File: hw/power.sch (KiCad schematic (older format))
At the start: 10 parts, among them U10 MCP1826S, U11 MCP1826S

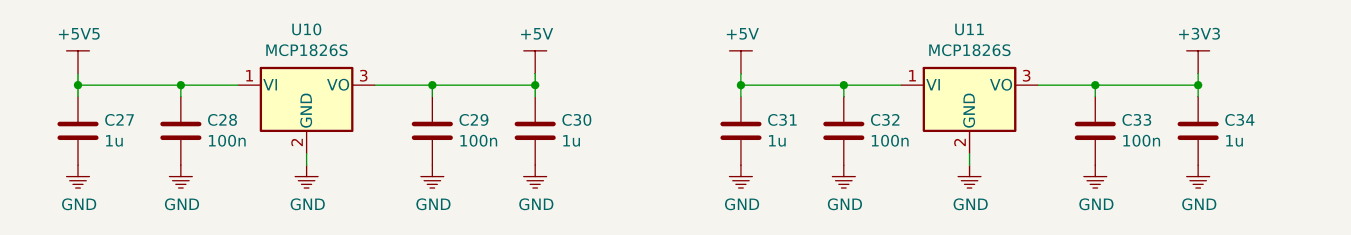
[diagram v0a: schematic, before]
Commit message: updated schematic added footptints
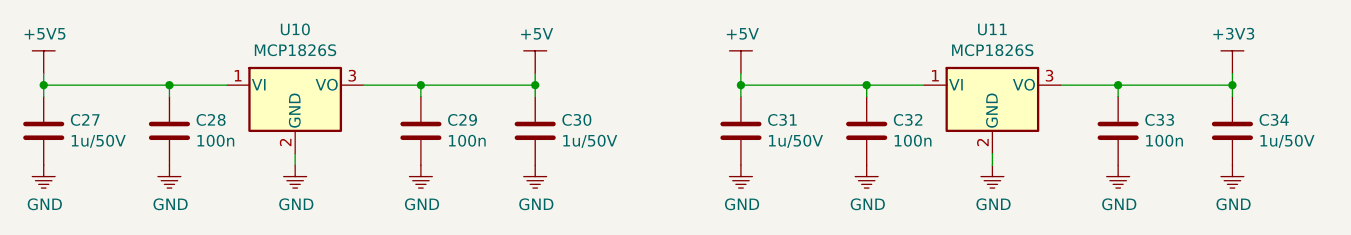
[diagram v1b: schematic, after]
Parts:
- C27, C30, C31, C34: value 1u -> 1u/50V; footprint (none) -> Capacitor_SMD:C_0805_2012Metric
- C28, C29, C32, C33: footprint (none) -> Capacitor_SMD:C_0805_2012Metric
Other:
- moved on the sheet: C27, C28, C29, C32, C33, C34, U10, U11

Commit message: updated schematic
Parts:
- renumbered U11 to U10, U10 to U9
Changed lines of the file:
@@
 $EndDescr
 $Comp
-L Regulator_Linear:MCP1826S U10
+L Regulator_Linear:MCP1826S U9
 U 1 1 5ACF90C5
 P 2650 2300
-F 0 "U10" H 2650 2542 50  0000 C CNN
+F 0 "U9" H 2650 2542 50  0000 C CNN
 F 1 "MCP1826S" H 2650 2451 50  0000 C CNN
 F 2 "Package_TO_SOT_SMD:SOT-223-3_TabPin2" H 2550 2450 50  0001 C CNN
@@
 $EndComp
 $Comp
-L KLIB_Power:GND #PWR068
+L KLIB_Power:GND #PWR067
 U 1 1 5ACF90E8
 P 1550 2650
-F 0 "#PWR068" H 1550 2450 50  0001 C CNN
+F 0 "#PWR067" H 1550 2450 50  0001 C CNN
 F 1 "GND" H 1555 2477 50  0000 C CNN
 F 2 "" H 1550 2650 50  0001 C CNN
@@
 $EndComp
 $Comp
-L KLIB_Power:GND #PWR069
+L KLIB_Power:GND #PWR068
 U 1 1 5ACF90EE
 P 2100 2650
-F 0 "#PWR069" H 2100 2450 50  0001 C CNN
+F 0 "#PWR068" H 2100 2450 50  0001 C CNN
 F 1 "GND" H 2105 2477 50  0000 C CNN
 F 2 "" H 2100 2650 50  0001 C CNN
@@
 $EndComp
 $Comp
-L KLIB_Power:GND #PWR070
+L KLIB_Power:GND #PWR069
 U 1 1 5ACF90F4
 P 2650 2650
-F 0 "#PWR070" H 2650 2450 50  0001 C CNN
+F 0 "#PWR069" H 2650 2450 50  0001 C CNN
 F 1 "GND" H 2655 2477 50  0000 C CNN
 F 2 "" H 2650 2650 50  0001 C CNN
@@
 $EndComp
 $Comp
-L KLIB_Power:GND #PWR071
+L KLIB_Power:GND #PWR070
 U 1 1 5ACF90FA
 P 3200 2650
-F 0 "#PWR071" H 3200 2450 50  0001 C CNN
+F 0 "#PWR070" H 3200 2450 50  0001 C CNN
 F 1 "GND" H 3205 2477 50  0000 C CNN
 F 2 "" H 3200 2650 50  0001 C CNN
@@
 $EndComp
 $Comp
-L KLIB_Power:GND #PWR073
+L KLIB_Power:GND #PWR072
 U 1 1 5ACF9100
 P 3700 2650
-F 0 "#PWR073" H 3700 2450 50  0001 C CNN
+F 0 "#PWR072" H 3700 2450 50  0001 C CNN
 F 1 "GND" H 3705 2477 50  0000 C CNN
 F 2 "" H 3700 2650 50  0001 C CNN
@@
 Connection ~ 3700 2300
 $Comp
-L KLIB_Power:+5V #PWR072
+L KLIB_Power:+5V #PWR071
 U 1 1 5ACF9115
 P 3700 2250
-F 0 "#PWR072" H 3700 1950 50  0001 C CNN
+F 0 "#PWR071" H 3700 1950 50  0001 C CNN
 F 1 "+5V" H 3705 2423 50  0000 C CNN
 F 2 "" H 3700 2250 50  0001 C CNN
@@
 $EndComp
 $Comp
-L KLIB_Power:+5V5 #PWR067
+L KLIB_Power:+5V5 #PWR066
 U 1 1 5ACF911B
 P 1550 2250
-F 0 "#PWR067" H 1550 1950 50  0001 C CNN
+F 0 "#PWR066" H 1550 1950 50  0001 C CNN
 F 1 "+5V5" H 1555 2423 50  0000 C CNN
 F 2 "" H 1550 2250 50  0001 C CNN
@@
 $EndComp
 $Comp
-L Regulator_Linear:MCP1826S U11
+L Regulator_Linear:MCP1826S U10
 U 1 1 5ACF9121
 P 5700 2300
-F 0 "U11" H 5700 2542 50  0000 C CNN
+F 0 "U10" H 5700 2542 50  0000 C CNN
 F 1 "MCP1826S" H 5700 2451 50  0000 C CNN
 F 2 "Package_TO_SOT_SMD:SOT-223-3_TabPin2" H 5600 2450 50  0001 C CNN
@@
 $EndComp
 $Comp
-L KLIB_Power:GND #PWR075
+L KLIB_Power:GND #PWR074
 U 1 1 5ACF9144
 P 4600 2650
-F 0 "#PWR075" H 4600 2450 50  0001 C CNN
+F 0 "#PWR074" H 4600 2450 50  0001 C CNN
 F 1 "GND" H 4605 2477 50  0000 C CNN
 F 2 "" H 4600 2650 50  0001 C CNN
@@
 $EndComp
 $Comp
-L KLIB_Power:GND #PWR076
+L KLIB_Power:GND #PWR075
 U 1 1 5ACF914A
 P 5150 2650
-F 0 "#PWR076" H 5150 2450 50  0001 C CNN
+F 0 "#PWR075" H 5150 2450 50  0001 C CNN
 F 1 "GND" H 5155 2477 50  0000 C CNN
 F 2 "" H 5150 2650 50  0001 C CNN
@@
 $EndComp
 $Comp
-L KLIB_Power:GND #PWR077
+L KLIB_Power:GND #PWR076
 U 1 1 5ACF9150
 P 5700 2650
-F 0 "#PWR077" H 5700 2450 50  0001 C CNN
+F 0 "#PWR076" H 5700 2450 50  0001 C CNN
 F 1 "GND" H 5705 2477 50  0000 C CNN
 F 2 "" H 5700 2650 50  0001 C CNN
@@
 $EndComp
 $Comp
-L KLIB_Power:GND #PWR078
+L KLIB_Power:GND #PWR077
 U 1 1 5ACF9156
 P 6250 2650
-F 0 "#PWR078" H 6250 2450 50  0001 C CNN
+F 0 "#PWR077" H 6250 2450 50  0001 C CNN
 F 1 "GND" H 6255 2477 50  0000 C CNN
 F 2 "" H 6250 2650 50  0001 C CNN
@@
 $EndComp
 $Comp
-L KLIB_Power:GND #PWR080
+L KLIB_Power:GND #PWR079
 U 1 1 5ACF915C
 P 6750 2650
-F 0 "#PWR080" H 6750 2450 50  0001 C CNN
+F 0 "#PWR079" H 6750 2450 50  0001 C CNN
 F 1 "GND" H 6755 2477 50  0000 C CNN
 F 2 "" H 6750 2650 50  0001 C CNN
@@
 Connection ~ 6750 2300
 $Comp
-L KLIB_Power:+5V #PWR074
+L KLIB_Power:+5V #PWR073
 U 1 1 5ACF9171
 P 4600 2250
-F 0 "#PWR074" H 4600 1950 50  0001 C CNN
+F 0 "#PWR073" H 4600 1950 50  0001 C CNN
 F 1 "+5V" H 4605 2423 50  0000 C CNN
 F 2 "" H 4600 2250 50  0001 C CNN
@@
 $EndComp
 $Comp
-L KLIB_Power:+3V3 #PWR079
+L KLIB_Power:+3V3 #PWR078
 U 1 1 5ACF9177
 P 6750 2250
-F 0 "#PWR079" H 6750 1950 50  0001 C CNN
+F 0 "#PWR078" H 6750 1950 50  0001 C CNN
 F 1 "+3V3" H 6755 2423 50  0000 C CNN
 F 2 "" H 6750 2250 50  0001 C CNN
